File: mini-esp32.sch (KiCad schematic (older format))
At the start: 52 parts, among them J1 BAT, J2 USB_B_Micro, J5 Conn_01x18, J6 Conn_01x18, Q1 AO3401A, Q2 S8050, Q3 S8050, Q5 AO3400A, Q6 AO3400A, SW1 RESET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

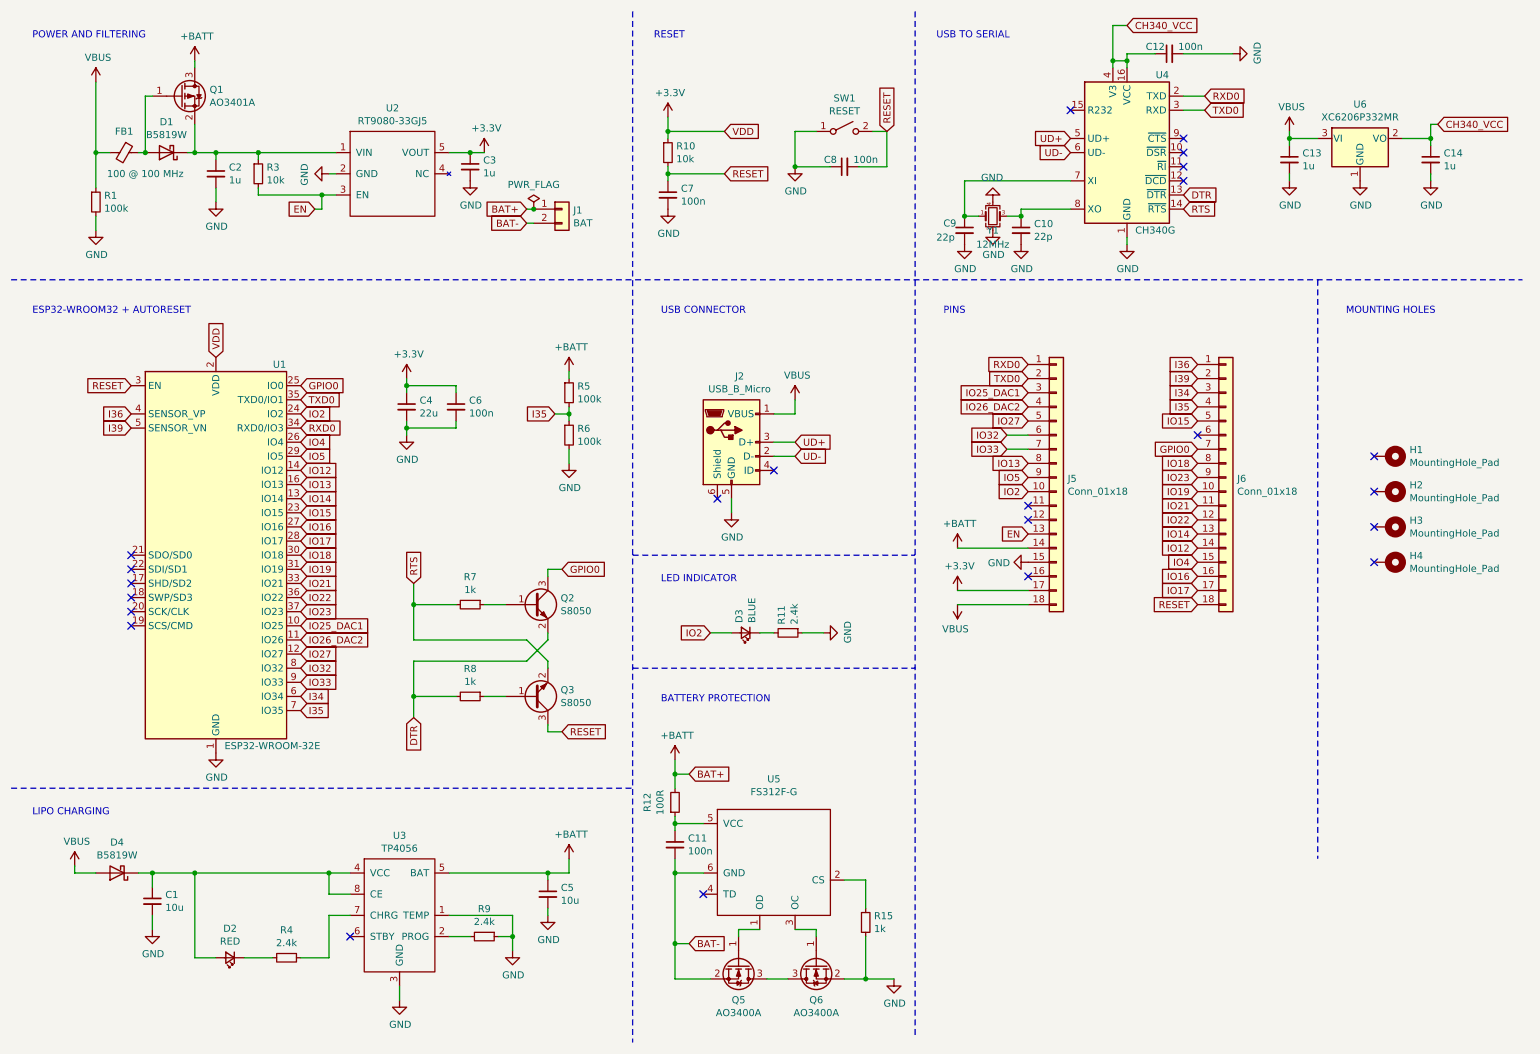
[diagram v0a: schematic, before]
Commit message: Add comments in the schematic
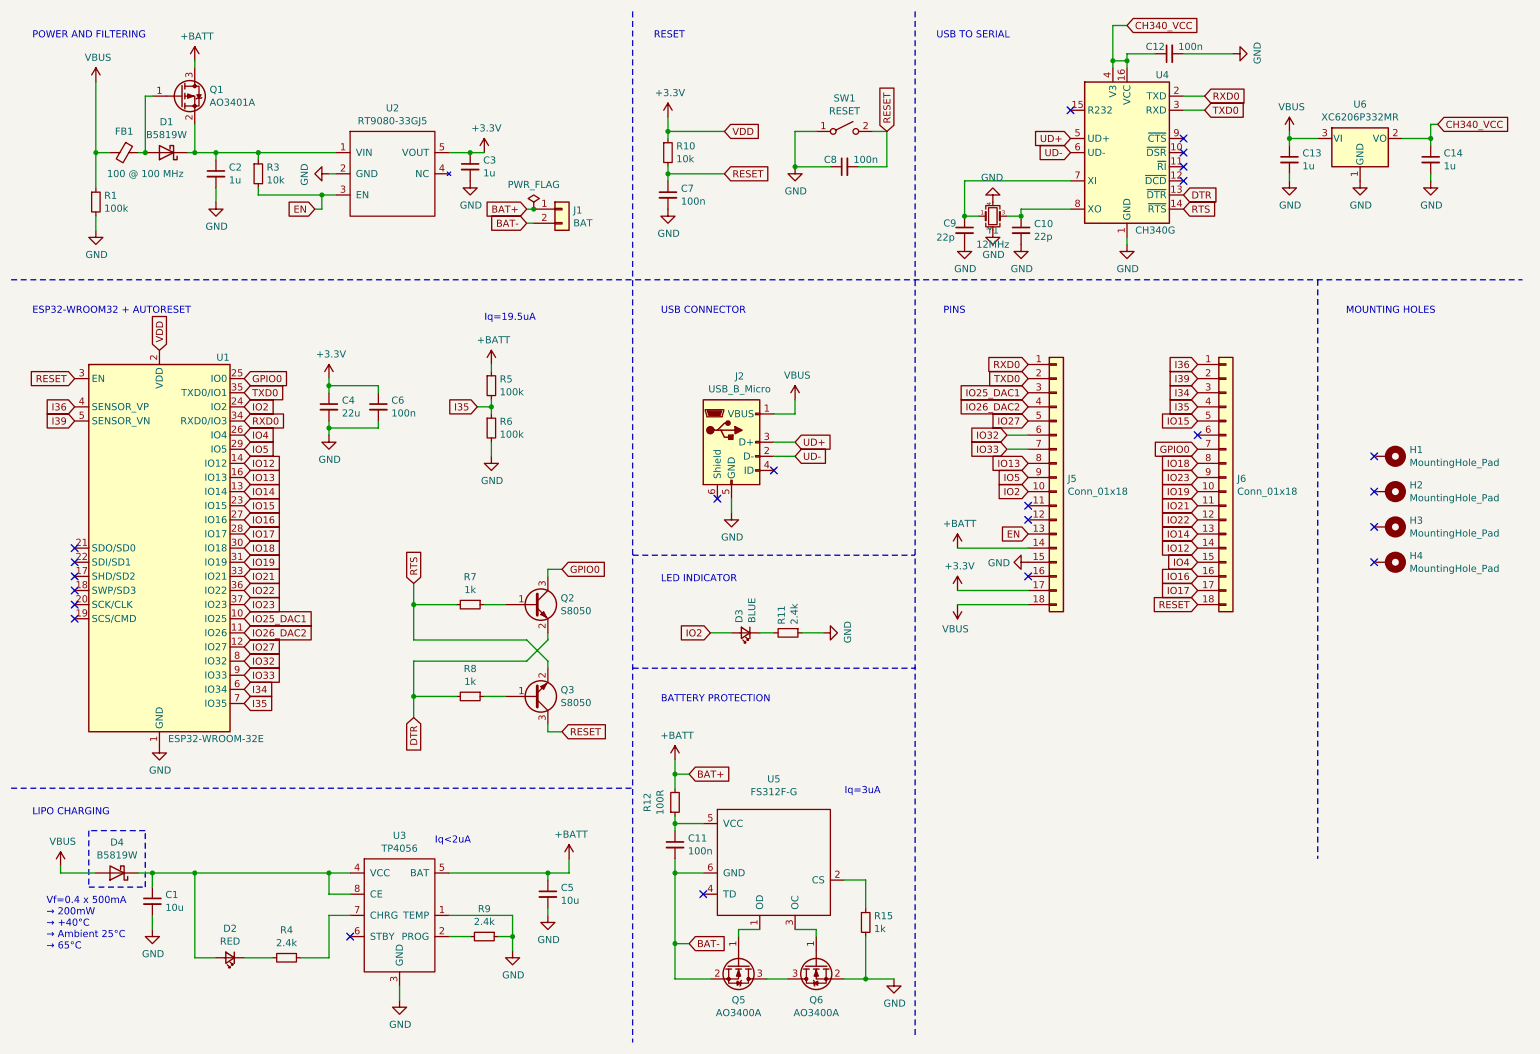
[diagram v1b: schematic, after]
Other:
- note added: "Iq<2uA"
- note added: "Iq=19.5uA"
- note added: "Iq=3uA"
- note added: "Vf=0.4 x 500mA\n→ 200mW\n→ +40°C\n→ Ambient 25°C\n→ 65°C"
- moved on the sheet: C4, C6, R5, R6, U1

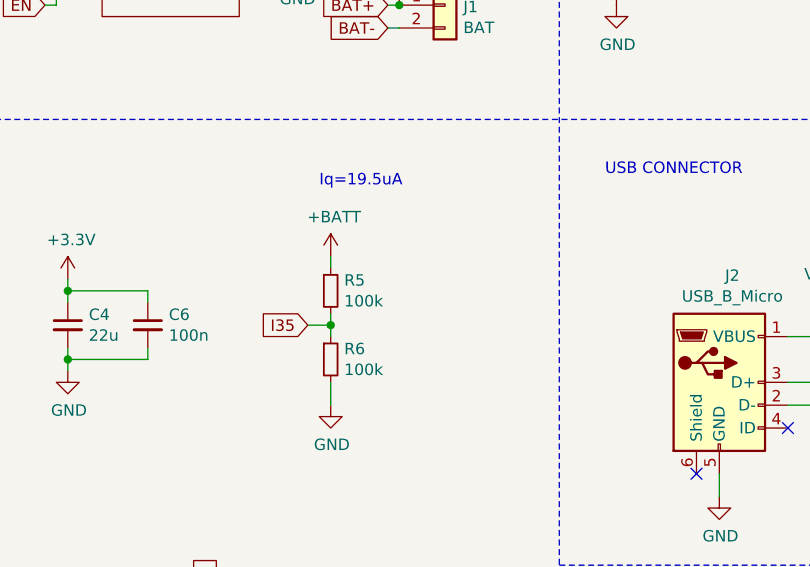
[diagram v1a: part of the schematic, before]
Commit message: Lower leakage current on battery voltage divider. Add caps.
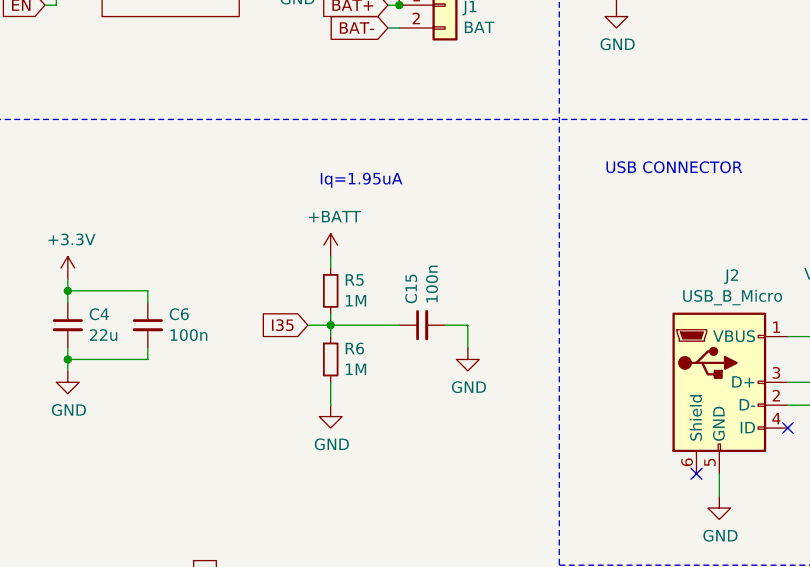
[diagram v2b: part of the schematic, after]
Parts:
- added C15: 100n, Capacitor_SMD:C_0402_1005Metric, symbol Device:C_Small
- R5, R6: value 100k -> 1M; LCSC Part # C25741 -> C26083
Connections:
- net GND: now also C15.2
- net I35: now also C15.1
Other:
- note added: "Iq=1.95uA"
- note removed: "Iq=19.5uA"
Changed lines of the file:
@@
 P 3900 3150
 F 0 "R5" H 3959 3196 50  0000 L CNN
-F 1 "100k" H 3959 3105 50  0000 L CNN
+F 1 "1M" H 3959 3105 50  0000 L CNN
 F 2 "Resistor_SMD:R_0402_1005Metric" H 3900 3150 50  0001 C CNN
 F 3 "~" H 3900 3150 50  0001 C CNN
-F 4 "C25741" H 3900 3150 50  0001 C CNN "LCSC Part #"
+F 4 "C26083" H 3900 3150 50  0001 C CNN "LCSC Part #"
 	1    3900 3150
 	1    0    0    -1
@@
 P 3900 3450
 F 0 "R6" H 3959 3496 50  0000 L CNN
-F 1 "100k" H 3959 3405 50  0000 L CNN
+F 1 "1M" H 3959 3405 50  0000 L CNN
 F 2 "Resistor_SMD:R_0402_1005Metric" H 3900 3450 50  0001 C CNN
 F 3 "~" H 3900 3450 50  0001 C CNN
-F 4 "C25741" H 3900 3450 50  0001 C CNN "LCSC Part #"
+F 4 "C26083" H 3900 3450 50  0001 C CNN "LCSC Part #"
 	1    3900 3450
 	1    0    0    -1
@@
 Iq<2uA
 Text Notes 3850 2700 0    50   ~ 0
-Iq=19.5uA
+Iq=1.95uA
+$Comp
+L Device:C_Small C15
+U 1 1 5FD2CC74
+P 4300 3300
+F 0 "C15" H 4392 3346 50  0000 L CNN
+F 1 "100n" H 4392 3255 50  0000 L CNN
+F 2 "Capacitor_SMD:C_0402_1005Metric" H 4300 3300 50  0001 C CNN
+F 3 "~" H 4300 3300 50  0001 C CNN
+F 4 "C1525" H 4300 3300 50  0001 C CNN "LCSC Part #"
+	1    4300 3300
+	0    -1   -1   0
+$EndComp
+$Comp
+L power:GND #PWR07
+U 1 1 5FD2E46C
+P 4500 3400
+F 0 "#PWR07" H 4500 3150 50  0001 C CNN
+F 1 "GND" H 4505 3227 50  0000 C CNN
+F 2 "" H 4500 3400 50  0001 C CNN
+F 3 "" H 4500 3400 50  0001 C CNN
+	1    4500 3400
+	1    0    0    -1
+$EndComp
+Wire Wire Line
+	4500 3400 4500 3300
+Wire Wire Line
+	4500 3300 4400 3300
+Wire Wire Line
+	4200 3300 3900 3300
 $EndSCHEMATC

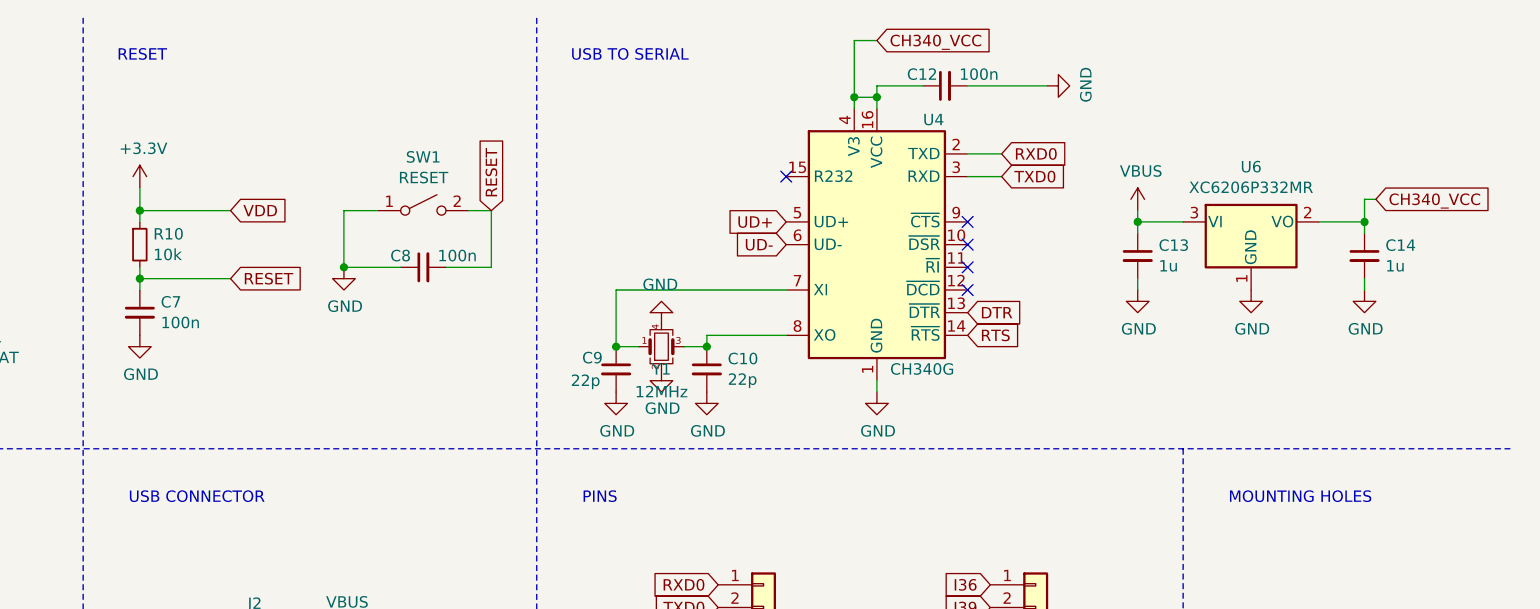
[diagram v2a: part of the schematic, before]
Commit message: Fix EN pin cap to increase startup delay. Cheaper main bulk cap.
Improve thermals for D4 diode. (For charging)
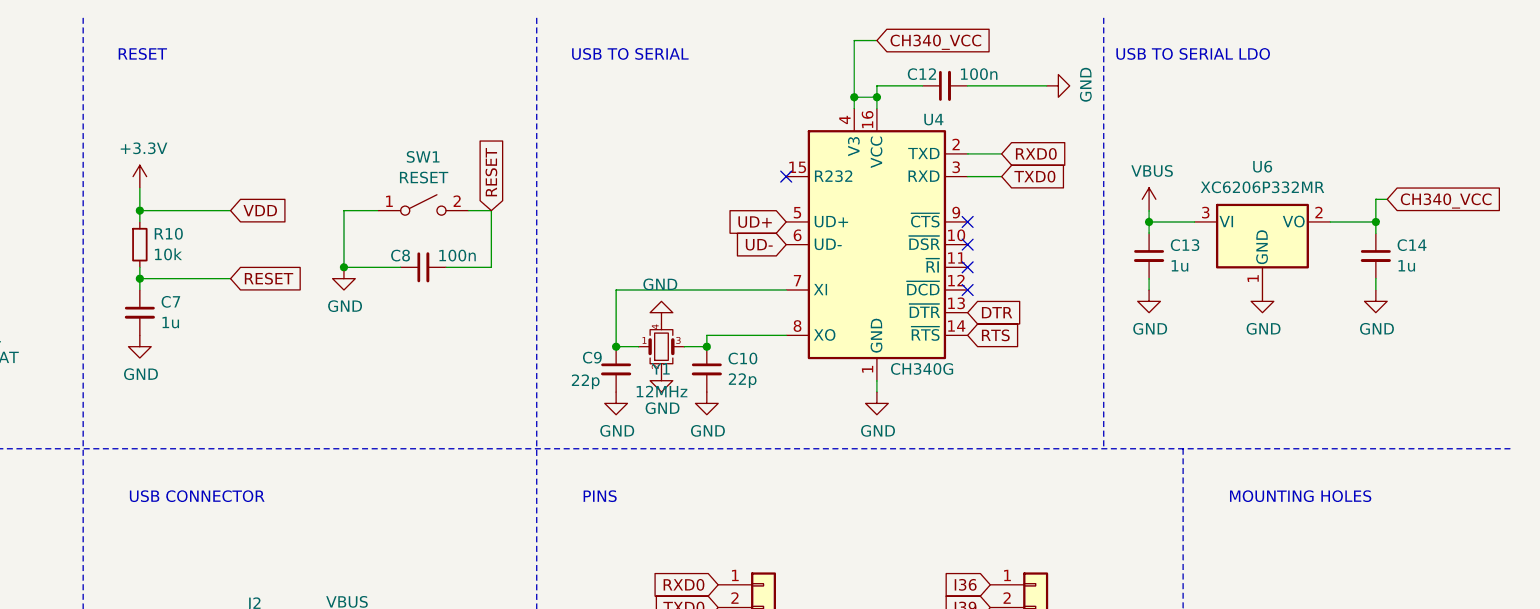
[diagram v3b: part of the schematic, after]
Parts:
- C4: footprint Capacitor_SMD:C_0805_2012Metric -> Capacitor_SMD:C_0603_1608Metric; LCSC Part # C45783 -> C59461
- C7: value 100n -> 1u; LCSC Part # C1525 -> C52923
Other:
- note added: "USB TO SERIAL LDO"
- moved on the sheet: C13, C14, U6
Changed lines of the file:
@@
 F 0 "C4" H 2842 3346 50  0000 L CNN
 F 1 "22u" H 2842 3255 50  0000 L CNN
-F 2 "Capacitor_SMD:C_0805_2012Metric" H 2750 3300 50  0001 C CNN
+F 2 "Capacitor_SMD:C_0603_1608Metric" H 2750 3300 50  0001 C CNN
 F 3 "~" H 2750 3300 50  0001 C CNN
-F 4 "C45783" H 2750 3300 50  0001 C CNN "LCSC Part #"
+F 4 "C59461" H 2750 3300 50  0001 C CNN "LCSC Part #"
 	1    2750 3300
 	1    0    0    -1
@@
 F 4 "C25744" H 5150 1500 50  0001 C CNN "LCSC Part #"
 	1    5150 1500
-	1    0    0    -1
-$EndComp
-$Comp
-L Device:C_Small C7
-U 1 1 5F8363D3
-P 5150 1800
-F 0 "C7" H 5242 1846 50  0000 L CNN
-F 1 "100n" H 5242 1755 50  0000 L CNN
-F 2 "Capacitor_SMD:C_0402_1005Metric" H 5150 1800 50  0001 C CNN
-F 3 "~" H 5150 1800 50  0001 C CNN
-F 4 "C1525" H 5150 1800 50  0001 C CNN "LCSC Part #"
-	1    5150 1800
 	1    0    0    -1
 $EndComp
@@
 Wire Wire Line
 	5200 6250 5200 6200
-Connection ~ 10550 1400
-Wire Wire Line
-	10550 1300 10550 1400
-Wire Wire Line
-	10600 1300 10550 1300
-Wire Wire Line
-	9550 1650 9550 1700
-Wire Wire Line
-	10550 1650 10550 1700
+Connection ~ 10600 1400
+Wire Wire Line
+	10600 1300 10600 1400
+Wire Wire Line
+	10650 1300 10600 1300
+Wire Wire Line
+	9600 1650 9600 1700
+Wire Wire Line
+	10600 1650 10600 1700
 $Comp
 L power:GND #PWR06
 U 1 1 5FBA313D
-P 10550 1700
-F 0 "#PWR06" H 10550 1450 50  0001 C CNN
-F 1 "GND" H 10555 1527 50  0000 C CNN
-F 2 "" H 10550 1700 50  0001 C CNN
-F 3 "" H 10550 1700 50  0001 C CNN
-	1    10550 1700
+P 10600 1700
+F 0 "#PWR06" H 10600 1450 50  0001 C CNN
+F 1 "GND" H 10605 1527 50  0000 C CNN
+F 2 "" H 10600 1700 50  0001 C CNN
+F 3 "" H 10600 1700 50  0001 C CNN
+	1    10600 1700
 	1    0    0    -1
 $EndComp
@@
 L power:GND #PWR05
 U 1 1 5FBA2D40
-P 10050 1700
-F 0 "#PWR05" H 10050 1450 50  0001 C CNN
-F 1 "GND" H 10055 1527 50  0000 C CNN
-F 2 "" H 10050 1700 50  0001 C CNN
-F 3 "" H 10050 1700 50  0001 C CNN
-	1    10050 1700
+P 10100 1700
+F 0 "#PWR05" H 10100 1450 50  0001 C CNN
+F 1 "GND" H 10105 1527 50  0000 C CNN
+F 2 "" H 10100 1700 50  0001 C CNN
+F 3 "" H 10100 1700 50  0001 C CNN
+	1    10100 1700
 	1    0    0    -1
 $EndComp
@@
 L power:GND #PWR04
 U 1 1 5FBA2988
-P 9550 1700
-F 0 "#PWR04" H 9550 1450 50  0001 C CNN
-F 1 "GND" H 9555 1527 50  0000 C CNN
-F 2 "" H 9550 1700 50  0001 C CNN
-F 3 "" H 9550 1700 50  0001 C CNN
-	1    9550 1700
-	1    0    0    -1
-$EndComp
-Text GLabel 10600 1300 2    50   Input ~ 0
+P 9600 1700
+F 0 "#PWR04" H 9600 1450 50  0001 C CNN
+F 1 "GND" H 9605 1527 50  0000 C CNN
+F 2 "" H 9600 1700 50  0001 C CNN
+F 3 "" H 9600 1700 50  0001 C CNN
+	1    9600 1700
+	1    0    0    -1
+$EndComp
+Text GLabel 10650 1300 2    50   Input ~ 0
 CH340_VCC
 Wire Wire Line
-	10550 1400 10550 1450
-Wire Wire Line
-	10350 1400 10550 1400
-Connection ~ 9550 1400
-Wire Wire Line
-	9550 1400 9550 1450
-Wire Wire Line
-	9550 1400 9550 1350
-Wire Wire Line
-	9750 1400 9550 1400
+	10600 1400 10600 1450
+Wire Wire Line
+	10400 1400 10600 1400
+Connection ~ 9600 1400
+Wire Wire Line
+	9600 1400 9600 1450
+Wire Wire Line
+	9600 1400 9600 1350
+Wire Wire Line
+	9800 1400 9600 1400
 $Comp
 L Device:C_Small C14
 U 1 1 5FB42A74
-P 10550 1550
-F 0 "C14" H 10642 1596 50  0000 L CNN
-F 1 "1u" H 10642 1505 50  0000 L CNN
-F 2 "Capacitor_SMD:C_0402_1005Metric" H 10550 1550 50  0001 C CNN
-F 3 "~" H 10550 1550 50  0001 C CNN
-F 4 "C52923" H 10550 1550 50  0001 C CNN "LCSC Part #"
-	1    10550 1550
+P 10600 1550
+F 0 "C14" H 10692 1596 50  0000 L CNN
+F 1 "1u" H 10692 1505 50  0000 L CNN
+F 2 "Capacitor_SMD:C_0402_1005Metric" H 10600 1550 50  0001 C CNN
+F 3 "~" H 10600 1550 50  0001 C CNN
+F 4 "C52923" H 10600 1550 50  0001 C CNN "LCSC Part #"
+	1    10600 1550
 	1    0    0    -1
 $EndComp
@@
 L Device:C_Small C13
 U 1 1 5FB41A41
-P 9550 1550
-F 0 "C13" H 9642 1596 50  0000 L CNN
-F 1 "1u" H 9642 1505 50  0000 L CNN
-F 2 "Capacitor_SMD:C_0402_1005Metric" H 9550 1550 50  0001 C CNN
-F 3 "~" H 9550 1550 50  0001 C CNN
-F 4 "C52923" H 9550 1550 50  0001 C CNN "LCSC Part #"
-	1    9550 1550
+P 9600 1550
+F 0 "C13" H 9692 1596 50  0000 L CNN
+F 1 "1u" H 9692 1505 50  0000 L CNN
+F 2 "Capacitor_SMD:C_0402_1005Metric" H 9600 1550 50  0001 C CNN
+F 3 "~" H 9600 1550 50  0001 C CNN
+F 4 "C52923" H 9600 1550 50  0001 C CNN "LCSC Part #"
+	1    9600 1550
 	1    0    0    -1
 $EndComp
@@
 L Regulator_Linear:XC6206PxxxMR U6
 U 1 1 5FB3F47D
-P 10050 1400
-F 0 "U6" H 10050 1642 50  0000 C CNN
-F 1 "XC6206P332MR" H 10050 1551 50  0000 C CNN
-F 2 "Package_TO_SOT_SMD:SOT-23" H 10050 1625 50  0001 C CIN
-F 3 "https://www.torexsemi.com/file/xc6206/XC6206.pdf" H 10050 1400 50  0001 C CNN
-F 4 "C5446" H 10050 1400 50  0001 C CNN "LCSC Part #"
-	1    10050 1400
+P 10100 1400
+F 0 "U6" H 10100 1642 50  0000 C CNN
+F 1 "XC6206P332MR" H 10100 1551 50  0000 C CNN
+F 2 "Package_TO_SOT_SMD:SOT-23" H 10100 1625 50  0001 C CIN
+F 3 "https://www.torexsemi.com/file/xc6206/XC6206.pdf" H 10100 1400 50  0001 C CNN
+F 4 "C5446" H 10100 1400 50  0001 C CNN "LCSC Part #"
+	1    10100 1400
 	1    0    0    -1
 $EndComp
@@
 L power:VBUS #PWR0123
 U 1 1 5F9516D4
-P 9550 1350
-F 0 "#PWR0123" H 9550 1200 50  0001 C CNN
-F 1 "VBUS" H 9565 1523 50  0000 C CNN
-F 2 "" H 9550 1350 50  0001 C CNN
-F 3 "" H 9550 1350 50  0001 C CNN
-	1    9550 1350
+P 9600 1350
+F 0 "#PWR0123" H 9600 1200 50  0001 C CNN
+F 1 "VBUS" H 9615 1523 50  0000 C CNN
+F 2 "" H 9600 1350 50  0001 C CNN
+F 3 "" H 9600 1350 50  0001 C CNN
+	1    9600 1350
 	1    0    0    -1
 $EndComp
@@
 Wire Wire Line
 	4200 3300 3900 3300
+$Comp
+L Device:C_Small C7
+U 1 1 5F8363D3
+P 5150 1800
+F 0 "C7" H 5242 1846 50  0000 L CNN
+F 1 "1u" H 5242 1755 50  0000 L CNN
+F 2 "Capacitor_SMD:C_0402_1005Metric" H 5150 1800 50  0001 C CNN
+F 3 "~" H 5150 1800 50  0001 C CNN
+F 4 "C52923" H 5150 1800 50  0001 C CNN "LCSC Part #"
+	1    5150 1800
+	1    0    0    -1
+$EndComp
+Text Notes 9450 700  0    50   ~ 0
+USB TO SERIAL LDO
+Wire Notes Line
+	9400 500  9400 2400
 $EndSCHEMATC

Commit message: Inspection. Tuning. Gerber & assembly files.
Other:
- note added: "Iq = Typ 2uA / Max 4uA\nDropout V = Typ 0.31V / Max 0.53V"
- note added: "Iq=3uA\nOC=4.250V\nOD=2.90V"
- note added: "VCC = 2.3 - 3.6 V"
- note removed: "Iq=3uA"
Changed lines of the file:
@@
 Text Notes 750  7150 0    50   ~ 0
 Vf=0.4 x 500mA\n→ 200mW\n→ +40°C\n→ Ambient 25°C\n→ 65°C
-Text Notes 6400 6050 0    50   ~ 0
-Iq=3uA
+Text Notes 5500 5700 0    50   ~ 0
+Iq=3uA\nOC=4.250V\nOD=2.90V
 Wire Notes Line
 	1050 6300 1050 6700
@@
 Wire Notes Line
 	9400 500  9400 2400
+Text Notes 2900 1050 0    50   ~ 0
+Iq = Typ 2uA / Max 4uA\nDropout V = Typ 0.31V / Max 0.53V
+Text Notes 1700 2800 0    50   ~ 0
+VCC = 2.3 - 3.6 V
 $EndSCHEMATC
